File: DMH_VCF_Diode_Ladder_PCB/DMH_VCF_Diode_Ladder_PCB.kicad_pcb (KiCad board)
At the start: 2 copper layers, 96 x 175 mm, 0 parts

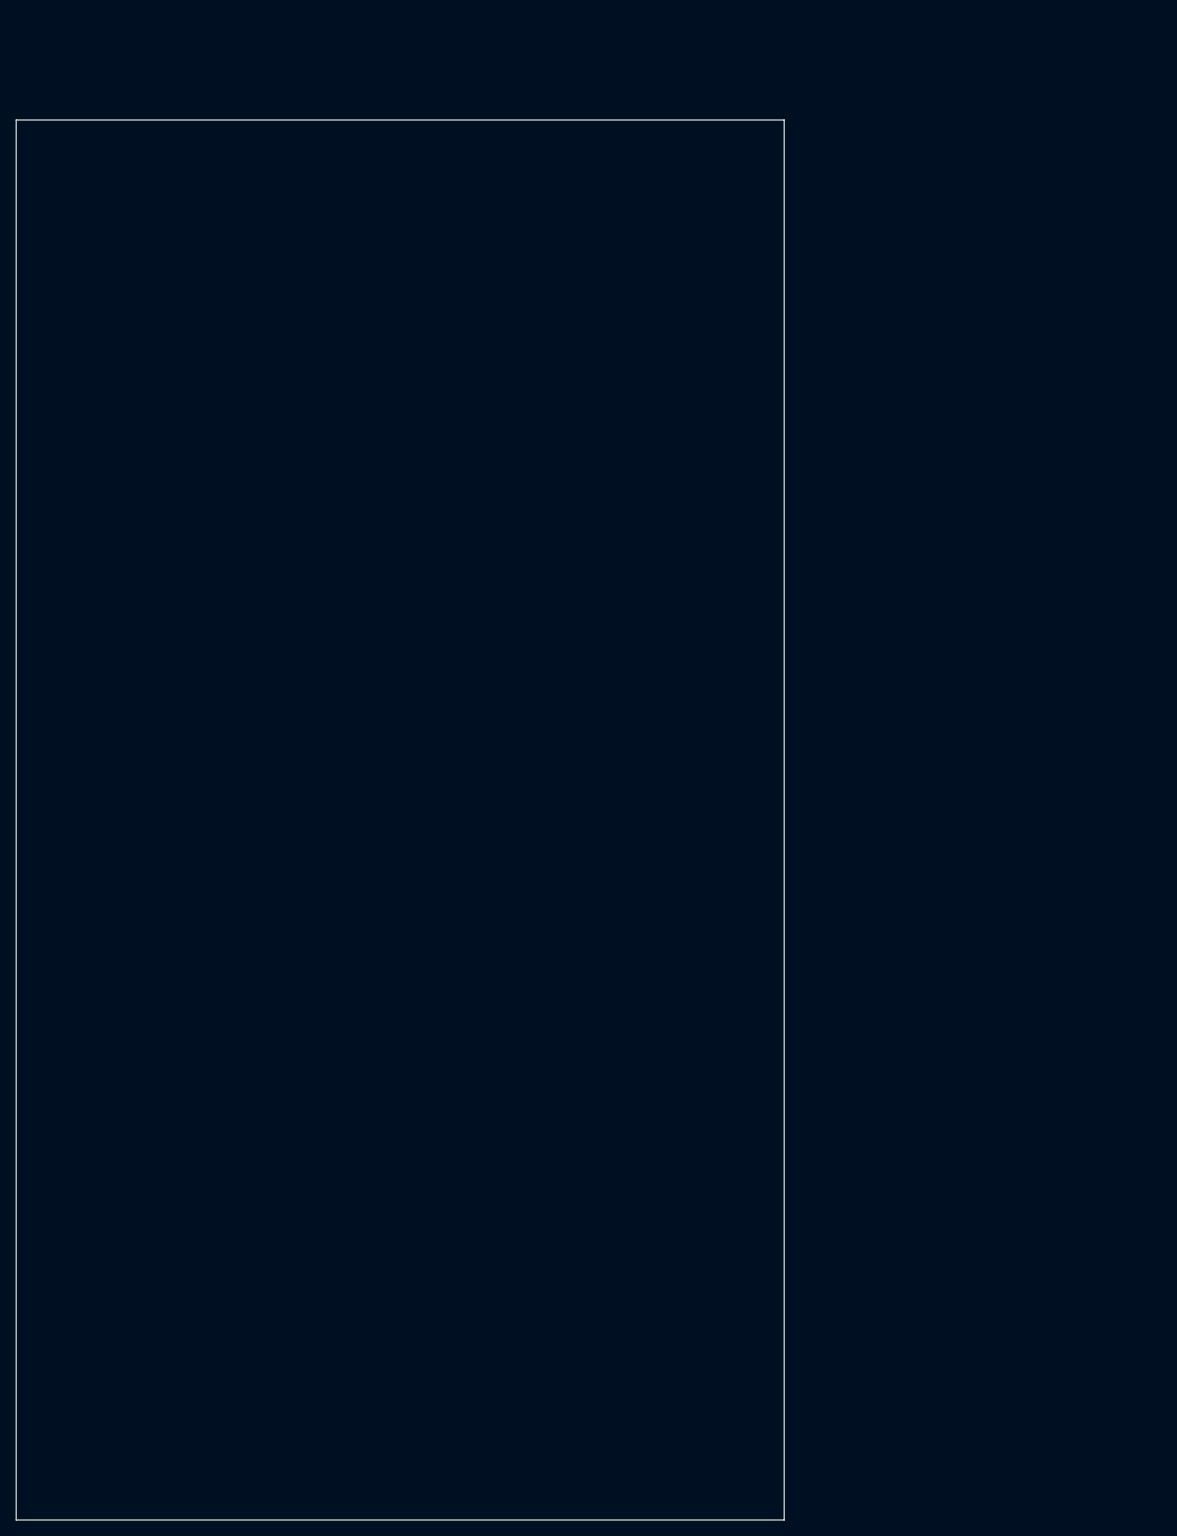
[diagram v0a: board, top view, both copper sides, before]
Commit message: Component placement in progress
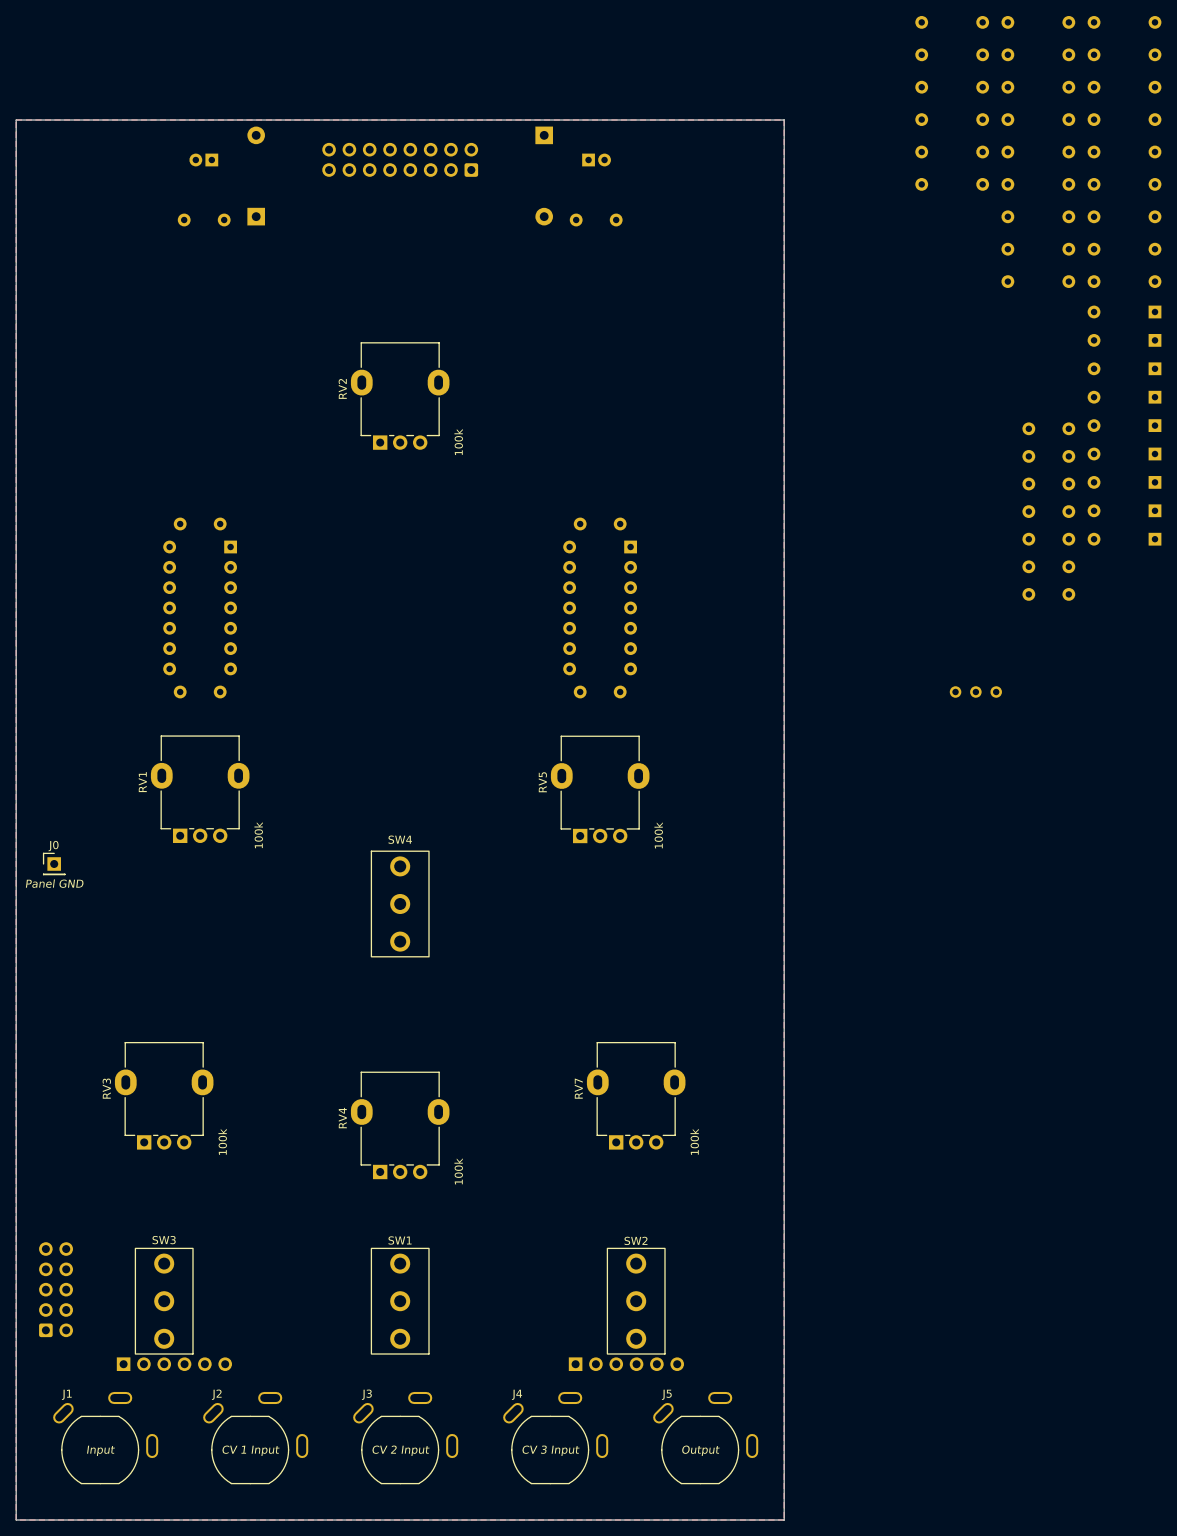
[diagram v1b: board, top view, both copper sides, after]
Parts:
- added C1: 47uF, Capacitor_THT:CP_Radial_D5.0mm_P2.00mm, B.Cu at (76.5, 47.5)
- added C10: 1nF, Capacitor_THT:C_Disc_D4.3mm_W1.9mm_P5.00mm, B.Cu at (183.6, 84.5)
- added C11: 1nF, Capacitor_THT:C_Disc_D4.3mm_W1.9mm_P5.00mm, B.Cu at (183.6, 88.0)
- added C12: 1nF, Capacitor_THT:C_Disc_D4.3mm_W1.9mm_P5.00mm, B.Cu at (183.6, 91.5)
- added C13: 1nF, Capacitor_THT:C_Disc_D4.3mm_W1.9mm_P5.00mm, B.Cu at (183.6, 94.9)
- added C14: 1nF, Capacitor_THT:C_Disc_D4.3mm_W1.9mm_P5.00mm, B.Cu at (183.6, 98.3)
- added C15: 1uF, Capacitor_THT:C_Disc_D4.3mm_W1.9mm_P5.00mm, B.Cu at (183.6, 101.8)
- added C16: 100nF, Capacitor_THT:C_Disc_D4.3mm_W1.9mm_P5.00mm, B.Cu at (127.5, 93.0)
- added C17: 100nF, Capacitor_THT:C_Disc_D4.3mm_W1.9mm_P5.00mm, B.Cu at (127.5, 114.0)
- added C2: 47uF, Capacitor_THT:CP_Radial_D5.0mm_P2.00mm, B.Cu at (123.5, 47.5)
- added C4: 100nF, Capacitor_THT:C_Disc_D4.3mm_W1.9mm_P5.00mm, B.Cu at (78.0, 55.0)
- added C5: 100nF, Capacitor_THT:C_Disc_D4.3mm_W1.9mm_P5.00mm, B.Cu at (127.0, 55.0)
- added C7: 1uF, Capacitor_THT:C_Disc_D4.3mm_W1.9mm_P5.00mm, B.Cu at (183.6, 81.1)
- added C8: 100nF, Capacitor_THT:C_Disc_D4.3mm_W1.9mm_P5.00mm, B.Cu at (77.5, 93.0)
- added C9: 100nF, Capacitor_THT:C_Disc_D4.3mm_W1.9mm_P5.00mm, B.Cu at (77.5, 114.0)
- added D1: SB140+, Diode_THT:D_DO-41_SOD81_P10.16mm_Horizontal, B.Cu at (82.0, 54.6)
- added D10: 1N4148, Diode_THT:D_DO-35_SOD27_P7.62mm_Horizontal, B.Cu at (194.3, 80.7)
- added D11: 1N4148, Diode_THT:D_DO-35_SOD27_P7.62mm_Horizontal, B.Cu at (194.3, 84.2)
- added D12: 1N4148, Diode_THT:D_DO-35_SOD27_P7.62mm_Horizontal, B.Cu at (194.3, 87.8)
- added D13: 1N4148, Diode_THT:D_DO-35_SOD27_P7.62mm_Horizontal, B.Cu at (194.3, 91.3)
- added D14: 1N4148, Diode_THT:D_DO-35_SOD27_P7.62mm_Horizontal, B.Cu at (194.3, 94.9)
- added D2: SB140-, Diode_THT:D_DO-41_SOD81_P10.16mm_Horizontal, B.Cu at (118.0, 44.4)
- added D6: 1N4148, Diode_THT:D_DO-35_SOD27_P7.62mm_Horizontal, B.Cu at (194.3, 66.5)
- added D7: 1N4148, Diode_THT:D_DO-35_SOD27_P7.62mm_Horizontal, B.Cu at (194.3, 70.0)
- added D8: 1N4148, Diode_THT:D_DO-35_SOD27_P7.62mm_Horizontal, B.Cu at (194.3, 73.6)
- added D9: 1N4148, Diode_THT:D_DO-35_SOD27_P7.62mm_Horizontal, B.Cu at (194.3, 77.2)
- added J0: Conn_01x01, Connector_PinHeader_2.54mm:PinHeader_1x01_P2.54mm_Vertical, F.Cu at (56.8, 135.5)
- added J1: TS_Jack_6.35mm_Sw, SynthStuff:CUI_MJ-63052A, F.Cu at (62.5, 208.8)
- added J100: IDC_02x08, SynthStuff:IDC-Header_2x08_P2.54mm_Vertical_Eurorack, B.Cu at (108.9, 48.8)
- added J2: TS_Jack_6.35mm_Sw, SynthStuff:CUI_MJ-63052A, F.Cu at (81.2, 208.8)
- added J200: IDC_02x05, SynthStuff:IDC-Header_2x05_P2.54mm_Vertical_BackBone, B.Cu at (55.7, 193.8)
- added J3: TS_Jack_6.35mm_Sw, SynthStuff:CUI_MJ-63052A, F.Cu at (100.0, 208.8)
- added J4: TS_Jack_6.35mm_Sw, SynthStuff:CUI_MJ-63052A, F.Cu at (118.8, 208.8)
- added J5: TS_Jack_6.35mm_Sw, SynthStuff:CUI_MJ-63052A, F.Cu at (137.5, 208.8)
- added J50: Conn_01x06, Connector_PinSocket_2.54mm:PinSocket_1x06_P2.54mm_Vertical, B.Cu at (121.9, 198.0)
- added J60: Conn_01x06, Connector_PinSocket_2.54mm:PinSocket_1x06_P2.54mm_Vertical, B.Cu at (65.4, 198.0)
- added R1: 27k, Resistor_THT:R_Axial_DIN0207_L6.3mm_D2.5mm_P7.62mm_Horizontal, B.Cu at (194.3, 30.3)
- added R10: 33k, Resistor_THT:R_Axial_DIN0207_L6.3mm_D2.5mm_P7.62mm_Horizontal, B.Cu at (183.6, 30.3)
- added R11: 33k, Resistor_THT:R_Axial_DIN0207_L6.3mm_D2.5mm_P7.62mm_Horizontal, B.Cu at (183.6, 34.4)
- added R12: 33k, Resistor_THT:R_Axial_DIN0207_L6.3mm_D2.5mm_P7.62mm_Horizontal, B.Cu at (183.6, 38.4)
- added R13: 33k, Resistor_THT:R_Axial_DIN0207_L6.3mm_D2.5mm_P7.62mm_Horizontal, B.Cu at (183.6, 42.5)
- added R14: 33k, Resistor_THT:R_Axial_DIN0207_L6.3mm_D2.5mm_P7.62mm_Horizontal, B.Cu at (183.6, 46.5)
- added R15: 33k, Resistor_THT:R_Axial_DIN0207_L6.3mm_D2.5mm_P7.62mm_Horizontal, B.Cu at (183.6, 50.5)
- added R16: 33k, Resistor_THT:R_Axial_DIN0207_L6.3mm_D2.5mm_P7.62mm_Horizontal, B.Cu at (183.6, 54.6)
- added R17: 2k, Resistor_THT:R_Axial_DIN0207_L6.3mm_D2.5mm_P7.62mm_Horizontal, B.Cu at (183.6, 58.6)
- added R18: 100k, Resistor_THT:R_Axial_DIN0207_L6.3mm_D2.5mm_P7.62mm_Horizontal, B.Cu at (183.6, 62.7)
- added R19: 1k, Resistor_THT:R_Axial_DIN0207_L6.3mm_D2.5mm_P7.62mm_Horizontal, B.Cu at (172.8, 30.3)
- added R2: 100k, Resistor_THT:R_Axial_DIN0207_L6.3mm_D2.5mm_P7.62mm_Horizontal, B.Cu at (194.3, 34.4)
- added R20: 1k, Resistor_THT:R_Axial_DIN0207_L6.3mm_D2.5mm_P7.62mm_Horizontal, B.Cu at (172.8, 34.4)
- added R21: 33k, Resistor_THT:R_Axial_DIN0207_L6.3mm_D2.5mm_P7.62mm_Horizontal, B.Cu at (172.8, 38.4)
- added R22: 100k, Resistor_THT:R_Axial_DIN0207_L6.3mm_D2.5mm_P7.62mm_Horizontal, B.Cu at (172.8, 42.5)
- added R23: 1k, Resistor_THT:R_Axial_DIN0207_L6.3mm_D2.5mm_P7.62mm_Horizontal, B.Cu at (172.8, 46.5)
- added R24: 68k, Resistor_THT:R_Axial_DIN0207_L6.3mm_D2.5mm_P7.62mm_Horizontal, B.Cu at (172.8, 50.5)
- added R3: 68k, Resistor_THT:R_Axial_DIN0207_L6.3mm_D2.5mm_P7.62mm_Horizontal, B.Cu at (194.3, 38.4)
- added R4: 68k, Resistor_THT:R_Axial_DIN0207_L6.3mm_D2.5mm_P7.62mm_Horizontal, B.Cu at (194.3, 42.5)
- added R5: 100k, Resistor_THT:R_Axial_DIN0207_L6.3mm_D2.5mm_P7.62mm_Horizontal, B.Cu at (194.3, 46.5)
- added R6: 2k, Resistor_THT:R_Axial_DIN0207_L6.3mm_D2.5mm_P7.62mm_Horizontal, B.Cu at (194.3, 50.5)
- added R7: 14k, Resistor_THT:R_Axial_DIN0207_L6.3mm_D2.5mm_P7.62mm_Horizontal, B.Cu at (194.3, 54.6)
- added R8: 27k, Resistor_THT:R_Axial_DIN0207_L6.3mm_D2.5mm_P7.62mm_Horizontal, B.Cu at (194.3, 58.6)
- added R9: 100k, Resistor_THT:R_Axial_DIN0207_L6.3mm_D2.5mm_P7.62mm_Horizontal, B.Cu at (194.3, 62.7)
- added RV1: 100k, SynthStuff:Potentiometer_Alpha_RD901F-40-00D_Single_Vertical, F.Cu at (72.5, 132.0)
- added RV2: 100k, SynthStuff:Potentiometer_Alpha_RD901F-40-00D_Single_Vertical, F.Cu at (97.5, 82.8)
- added RV3: 100k, SynthStuff:Potentiometer_Alpha_RD901F-40-00D_Single_Vertical, F.Cu at (68.0, 170.3)
- added RV4: 100k, SynthStuff:Potentiometer_Alpha_RD901F-40-00D_Single_Vertical, F.Cu at (97.5, 174.0)
- added RV5: 100k, SynthStuff:Potentiometer_Alpha_RD901F-40-00D_Single_Vertical, F.Cu at (122.5, 132.0)
- added RV6: 50k, Potentiometer_THT:Potentiometer_Bourns_3296W_Vertical, B.Cu at (169.4, 114.0)
- added RV7: 100k, SynthStuff:Potentiometer_Alpha_RD901F-40-00D_Single_Vertical, F.Cu at (127.0, 170.3)
- added SW1: SW_SPDT, SynthStuff:Toggle_Switch_THT, F.Cu at (100.0, 190.2)
- added SW2: SW_SPDT, SynthStuff:Toggle_Switch_THT, F.Cu at (129.5, 190.2)
- added SW3: SW_SPDT, SynthStuff:Toggle_Switch_THT, F.Cu at (70.5, 190.2)
- added SW4: SW_SPDT_321_OnOff, SynthStuff:Toggle_Switch_THT, F.Cu at (100.0, 140.5)
- added U1: TL074, Package_DIP:DIP-14_W7.62mm_Socket, B.Cu at (78.8, 95.9)
- added U2: TL074, Package_DIP:DIP-14_W7.62mm_Socket, B.Cu at (128.8, 95.9)
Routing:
- added copper zone on B.Cu, net GND
- added copper zone on F.Cu, net GND

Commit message: Component placement done
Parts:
- removed J1, J2, J3, J4, J5: TS_Jack_6.35mm_Sw, SynthStuff:CUI_MJ-63052A
- moved R3 172.2 mm to (79.0, 166.3), turned to 90 degrees
- moved R4 153.8 mm to (108.5, 170.0), turned to 90 degrees
- moved R8 150.5 mm to (56.0, 117.8), turned to 90 degrees
- moved R11 142.6 mm to (61.0, 107.3), turned to 90 degrees
- moved R9 141.6 mm to (61.0, 110.2), turned to -90 degrees
- moved D6 138.2 mm to (66.0, 117.8), turned to 90 degrees
- moved R7 136.0 mm to (66.0, 99.7), turned to -90 degrees
- moved R12 132.7 mm to (61.0, 89.2), turned to -90 degrees
- moved R13 129.5 mm to (66.0, 96.8), turned to 90 degrees
- moved R6 124.1 mm to (84.0, 107.3), turned to 90 degrees
- moved R5 121.6 mm to (89.0, 107.3), turned to 90 degrees
- moved R24 120.9 mm to (138.0, 166.3), turned to 90 degrees
- moved C7 120.8 mm to (75.5, 135.0), turned to 0 degrees
- moved R2 118.8 mm to (89.0, 89.2), turned to -90 degrees
- moved R1 116.4 mm to (94.0, 89.2), turned to -90 degrees
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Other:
- board size 96 x 175 mm -> 96 x 157.5 mm

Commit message: Routing in progress
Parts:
- moved C5 14.6 mm to (113.0, 59.2), turned to 0 degrees
- moved C4 5.84 mm to (82.0, 59.2), turned to 0 degrees
- moved C2 1.91 mm to (125.5, 47.5), turned to 180 degrees
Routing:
- net -12V: track 0.00 -> 111.6 mm
- net +12V: track 0.00 -> 80.6 mm
- net Net-(D1-A): track 0.00 -> 17.5 mm
- net Net-(D2-K): track 0.00 -> 12.4 mm
- net /Power/Bus Gate: track 0.00 -> 2.54 mm
- net /Inputs and Outputs/Bus CV In: track 0.00 -> 2.54 mm

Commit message: Routing in progress
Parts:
- moved R23 25.1 mm to (106.0, 95.7), turned to -90 degrees
- moved C10 1.39 mm to (123.0, 149.0)
- moved C11 1.39 mm to (127.5, 154.0)
- moved D8 1.39 mm to (125.5, 137.7)
- moved C12 1.39 mm to (132.6, 154.0)
- moved C13 1.39 mm to (137.6, 154.0)
- moved C14 1.39 mm to (142.1, 149.0)
- moved D10 1.39 mm to (135.0, 137.7)
- moved D11 1.39 mm to (139.7, 137.7)
- moved D12 1.39 mm to (144.6, 137.7)
- moved D7 1.39 mm to (120.8, 137.7)
- moved D9 1.39 mm to (130.3, 137.7)
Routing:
- net Net-(SW1-C): track 0.00 -> 167.8 mm
- net Net-(U1C--): track 0.00 -> 154.1 mm
- net Net-(SW3-B): track 0.00 -> 117.9 mm
- net /Core Circuit/Output: track 0.00 -> 108.9 mm
- net Net-(D13-K): track 0.00 -> 96.0 mm
- net -12V: track 111.6 -> 193.4 mm
- net Net-(SW1-B): track 0.00 -> 77.2 mm
- net /Core Circuit/CV1 Input: track 0.00 -> 77.0 mm
- net Net-(J60-Pin_3): track 0.00 -> 65.0 mm
- net +12V: track 80.6 -> 132.7 mm
- net Net-(D7-A): track 0.00 -> 43.1 mm
- net Net-(SW2-B): track 0.00 -> 40.6 mm
- net /Core Circuit/(Bus) CV2 Input: track 0.00 -> 34.5 mm
- net Net-(U2A-+): track 0.00 -> 33.5 mm
- net Net-(C7-Pad2): track 0.00 -> 31.2 mm
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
